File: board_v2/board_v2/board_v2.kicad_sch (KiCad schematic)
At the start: 34 parts, among them J1 Battery, J2 MOTR_SENS, J3 MOTL_SENS, J4 MOTL, J6 MOTR, U1 LD33V, U2 MPU-6050-Breakout, U3 DRV8313PWP, U5 DRV8313PWP

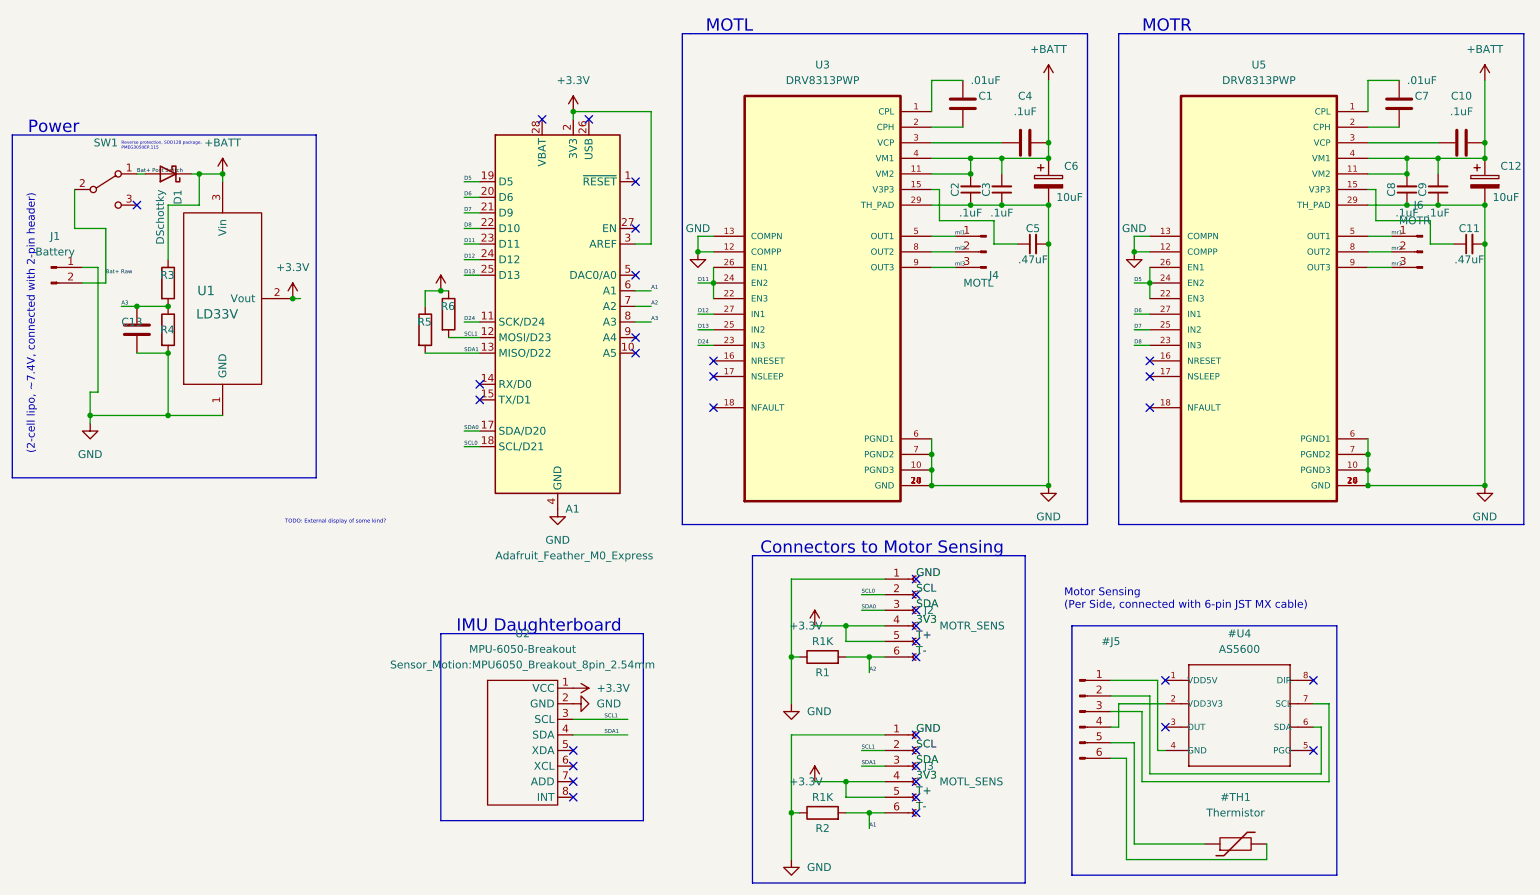
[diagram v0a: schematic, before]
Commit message: Update V2 board schematics
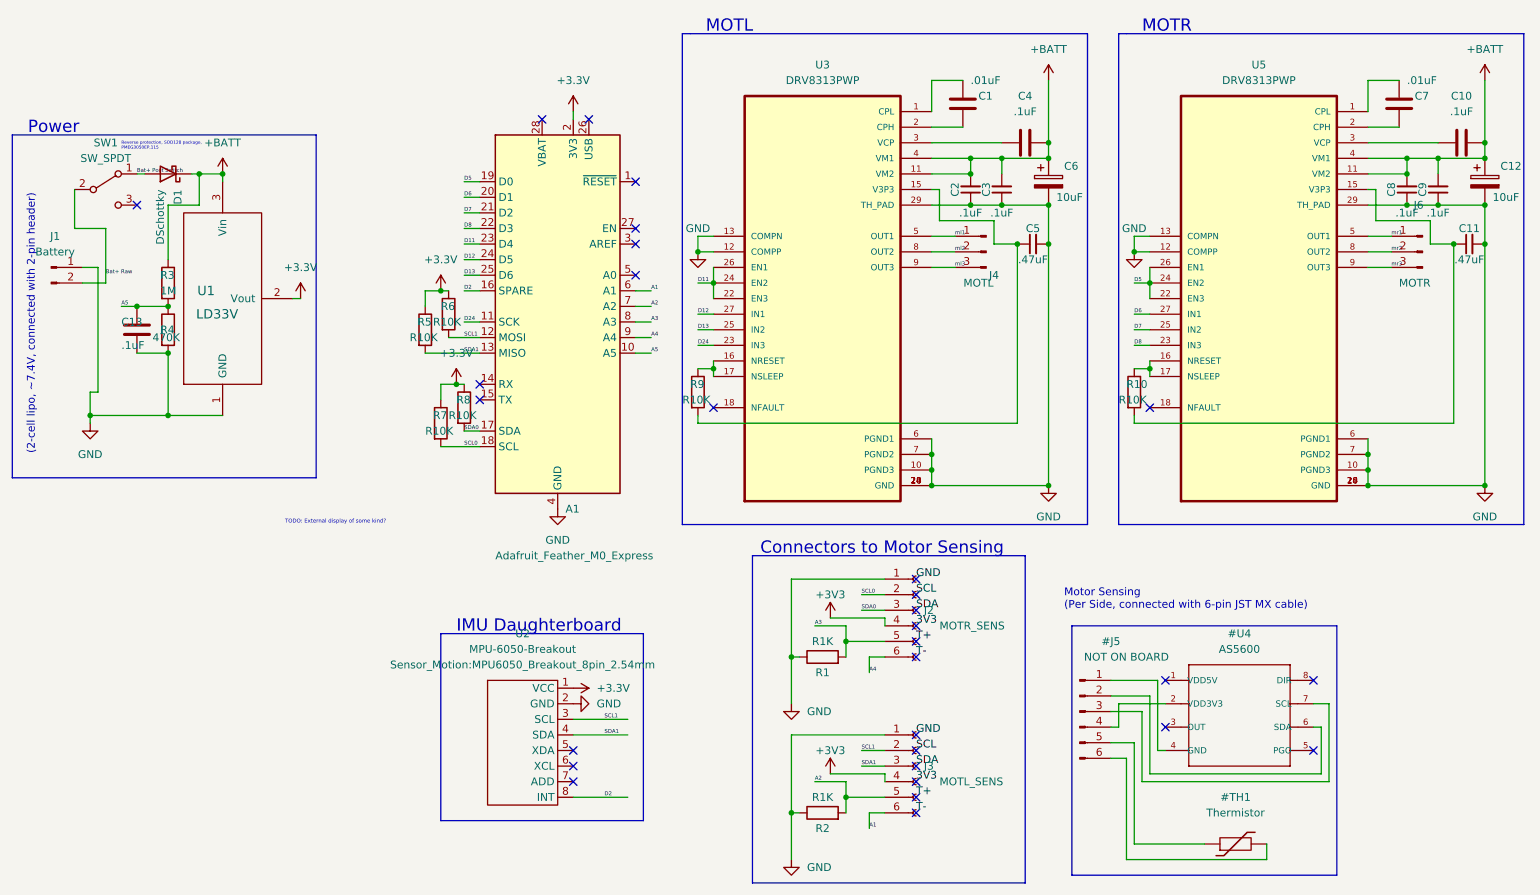
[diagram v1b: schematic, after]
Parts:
- added R10, R7, R8, R9: R10K, Resistor_SMD:R_0805_2012Metric_Pad1.20x1.40mm_HandSolder, symbol Device:R
- #J5: value (none) -> NOT ON BOARD
- A1: footprint Module:Adafruit_Feather_M0_Wifi_WithMountingHoles -> Module:Adafruit_Feather; symbol MCU_Module:Adafruit_Feather_M0_Express -> MCU_Module:Adafruit_Feather_Generic
- C13: value (none) -> .1uF; footprint (none) -> Capacitor_SMD:C_0805_2012Metric_Pad1.18x1.45mm_HandSolder
- R3: value (none) -> 1M; footprint (none) -> Resistor_SMD:R_0805_2012Metric_Pad1.20x1.40mm_HandSolder
- R4: value (none) -> 470K; footprint (none) -> Resistor_SMD:R_0805_2012Metric_Pad1.20x1.40mm_HandSolder
- R5, R6: value (none) -> R10K; footprint (none) -> Resistor_SMD:R_0805_2012Metric_Pad1.20x1.40mm_HandSolder
- SW1: value (none) -> SW_SPDT; footprint (none) -> downloaded:SW_L102021ML04Q
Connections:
- net +3V3: now also R7.1, R8.1; no longer A1.3 (AREF), J2.5 (Pin_5), J3.5 (Pin_5)
- net A1: no longer R2.2
- net A2: now also J3.5 (Pin_5), R2.2; no longer J2.6 (Pin_6), R1.2
- net A3: now also J2.5 (Pin_5), R1.2; no longer C13.1, R3.2, R4.1
- net GND: no longer A1.16 (GND)
- net SCL0: now also R7.2
- net SDA0: now also R8.2
- net A5: now reaches A1.10 (A5)
- net A5: now also C13.1, R3.2, R4.1
- net A4: now reaches A1.9 (A4)
- net A4: now also J2.6 (Pin_6)
- net D2: now reaches U2.8 (INT)
- net D2: now also A1.16 (SPARE)
- net at C11.1, U5.15 (V3P3): now also R10.2
- net at C5.1, U3.15 (V3P3): now also R9.2
- net at U3.16 (NRESET): now also U3.17 (NSLEEP), R9.1
- net at U5.16 (NRESET): now also U5.17 (NSLEEP), R10.1
- no-connect marks 36 -> 30
